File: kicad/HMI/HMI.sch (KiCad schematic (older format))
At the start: 38 parts

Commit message: Add files via upload
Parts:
- added R? (x6): 47k, symbol Device:R
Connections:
- net +3V3: now also R?.1, R?.1, R?.1, R?.1, R?.1, R?.1
- net R1: now also R?.2
- net R2: now also R?.2
- net R3: now also R?.2
- net R4: now also R?.2
- net R5: now also R?.2
- net R6: now also R?.2
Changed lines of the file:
@@
 	1    0    0    -1
 $EndComp
+Text GLabel 5900 2050 3    50   BiDi ~ 10
+R6
+$Comp
+L Device:R R?
+U 1 1 5E2A8493
+P 5900 1800
+F 0 "R?" H 5970 1846 50  0000 L CNN
+F 1 "47k" H 5970 1755 50  0000 L CNN
+F 2 "" V 5830 1800 50  0001 C CNN
+F 3 "~" H 5900 1800 50  0001 C CNN
+	1    5900 1800
+	1    0    0    -1
+$EndComp
+$Comp
+L power:+3.3V #PWR?
+U 1 1 5E2A8834
+P 5900 1450
+F 0 "#PWR?" H 5900 1300 50  0001 C CNN
+F 1 "+3.3V" H 5915 1623 50  0000 C CNN
+F 2 "" H 5900 1450 50  0001 C CNN
+F 3 "" H 5900 1450 50  0001 C CNN
+	1    5900 1450
+	1    0    0    -1
+$EndComp
+Text GLabel 6050 2050 3    50   BiDi ~ 10
+R5
+Text GLabel 6200 2050 3    50   BiDi ~ 10
+R4
+Text GLabel 6350 2050 3    50   BiDi ~ 10
+R3
+Text GLabel 6500 2050 3    50   BiDi ~ 10
+R2
+Text GLabel 6650 2050 3    50   BiDi ~ 10
+R1
+$Comp
+L Device:R R?
+U 1 1 5E2C0402
+P 6050 1800
+F 0 "R?" H 6120 1846 50  0000 L CNN
+F 1 "47k" H 6120 1755 50  0000 L CNN
+F 2 "" V 5980 1800 50  0001 C CNN
+F 3 "~" H 6050 1800 50  0001 C CNN
+	1    6050 1800
+	1    0    0    -1
+$EndComp
+$Comp
+L Device:R R?
+U 1 1 5E2C057A
+P 6200 1800
+F 0 "R?" H 6270 1846 50  0000 L CNN
+F 1 "47k" H 6270 1755 50  0000 L CNN
+F 2 "" V 6130 1800 50  0001 C CNN
+F 3 "~" H 6200 1800 50  0001 C CNN
+	1    6200 1800
+	1    0    0    -1
+$EndComp
+$Comp
+L Device:R R?
+U 1 1 5E2C0631
+P 6350 1800
+F 0 "R?" H 6420 1846 50  0000 L CNN
+F 1 "47k" H 6420 1755 50  0000 L CNN
+F 2 "" V 6280 1800 50  0001 C CNN
+F 3 "~" H 6350 1800 50  0001 C CNN
+	1    6350 1800
+	1    0    0    -1
+$EndComp
+$Comp
+L Device:R R?
+U 1 1 5E2C075F
+P 6500 1800
+F 0 "R?" H 6570 1846 50  0000 L CNN
+F 1 "47k" H 6570 1755 50  0000 L CNN
+F 2 "" V 6430 1800 50  0001 C CNN
+F 3 "~" H 6500 1800 50  0001 C CNN
+	1    6500 1800
+	1    0    0    -1
+$EndComp
+$Comp
+L Device:R R?
+U 1 1 5E2C0888
+P 6650 1800
+F 0 "R?" H 6720 1846 50  0000 L CNN
+F 1 "47k" H 6720 1755 50  0000 L CNN
+F 2 "" V 6580 1800 50  0001 C CNN
+F 3 "~" H 6650 1800 50  0001 C CNN
+	1    6650 1800
+	1    0    0    -1
+$EndComp
+Wire Wire Line
+	5900 2050 5900 1950
+Wire Wire Line
+	6050 1950 6050 2050
+Wire Wire Line
+	6200 2050 6200 1950
+Wire Wire Line
+	6350 1950 6350 2050
+Wire Wire Line
+	6500 2050 6500 1950
+Wire Wire Line
+	6650 1950 6650 2050
+Wire Wire Line
+	6650 1650 6650 1550
+Wire Wire Line
+	6650 1550 6500 1550
+Wire Wire Line
+	5900 1550 5900 1450
+Wire Wire Line
+	5900 1650 5900 1550
+Connection ~ 5900 1550
+Wire Wire Line
+	6050 1550 6050 1650
+Connection ~ 6050 1550
+Wire Wire Line
+	6050 1550 5900 1550
+Wire Wire Line
+	6200 1550 6200 1650
+Connection ~ 6200 1550
+Wire Wire Line
+	6200 1550 6050 1550
+Wire Wire Line
+	6350 1550 6350 1650
+Connection ~ 6350 1550
+Wire Wire Line
+	6350 1550 6200 1550
+Wire Wire Line
+	6500 1550 6500 1650
+Connection ~ 6500 1550
+Wire Wire Line
+	6500 1550 6350 1550
 $EndSCHEMATC

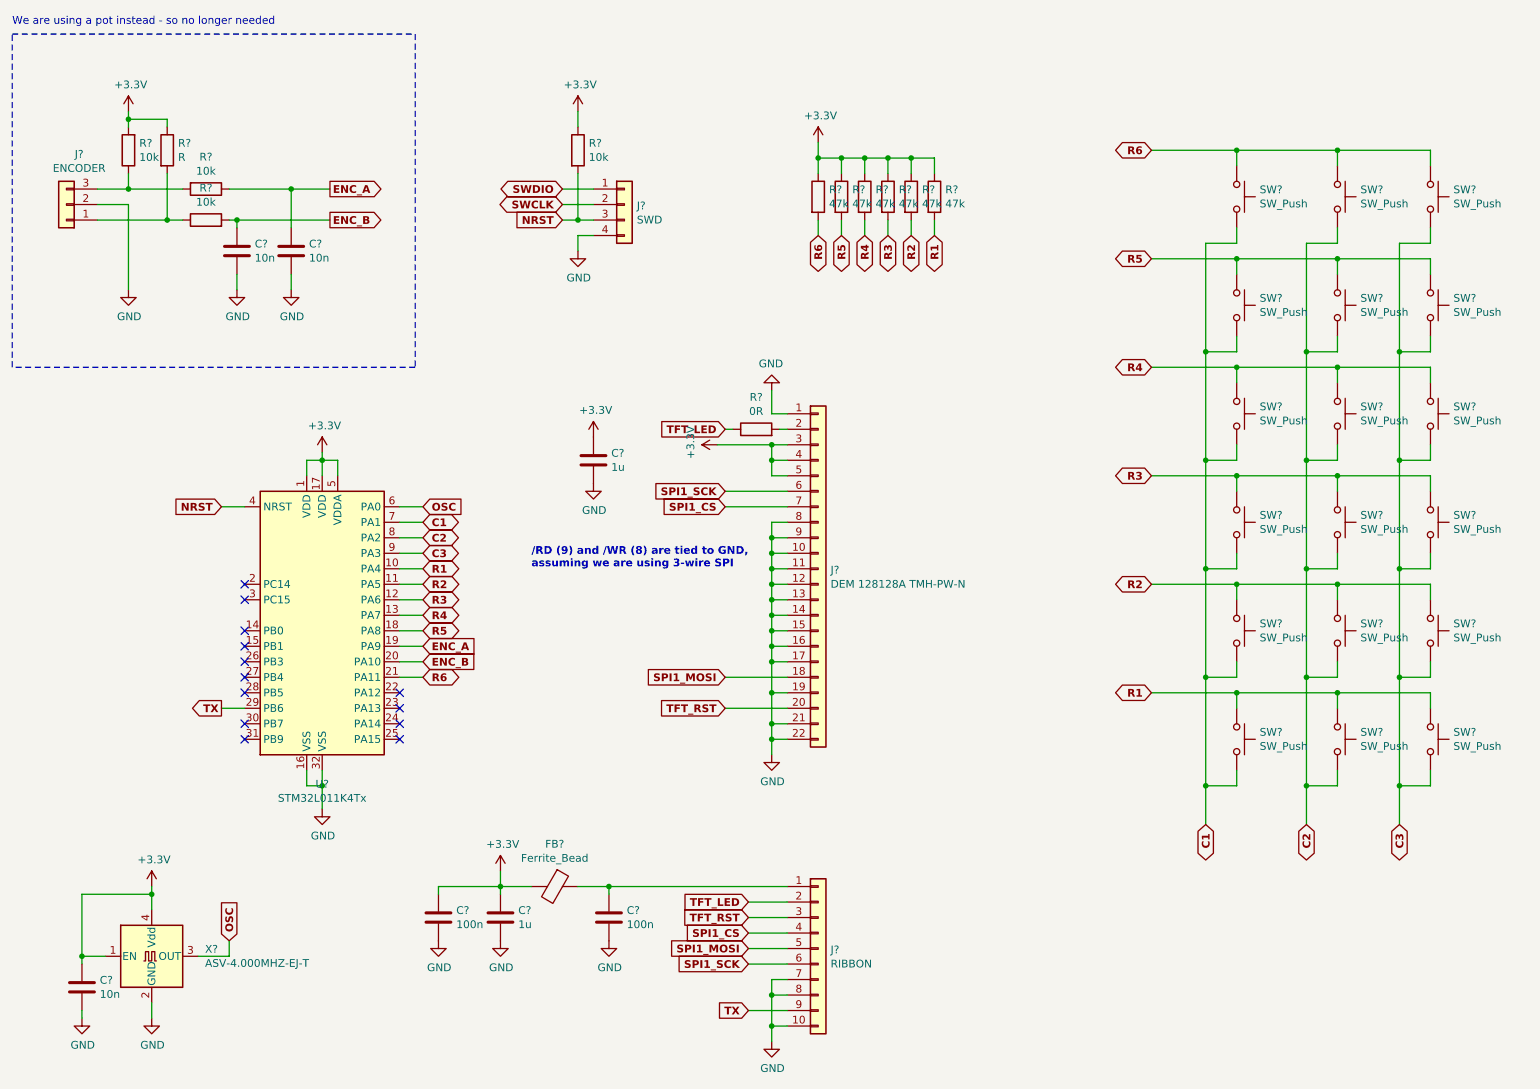
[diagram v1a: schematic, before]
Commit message: Add files via upload
added 2 buttons: F1 and F2
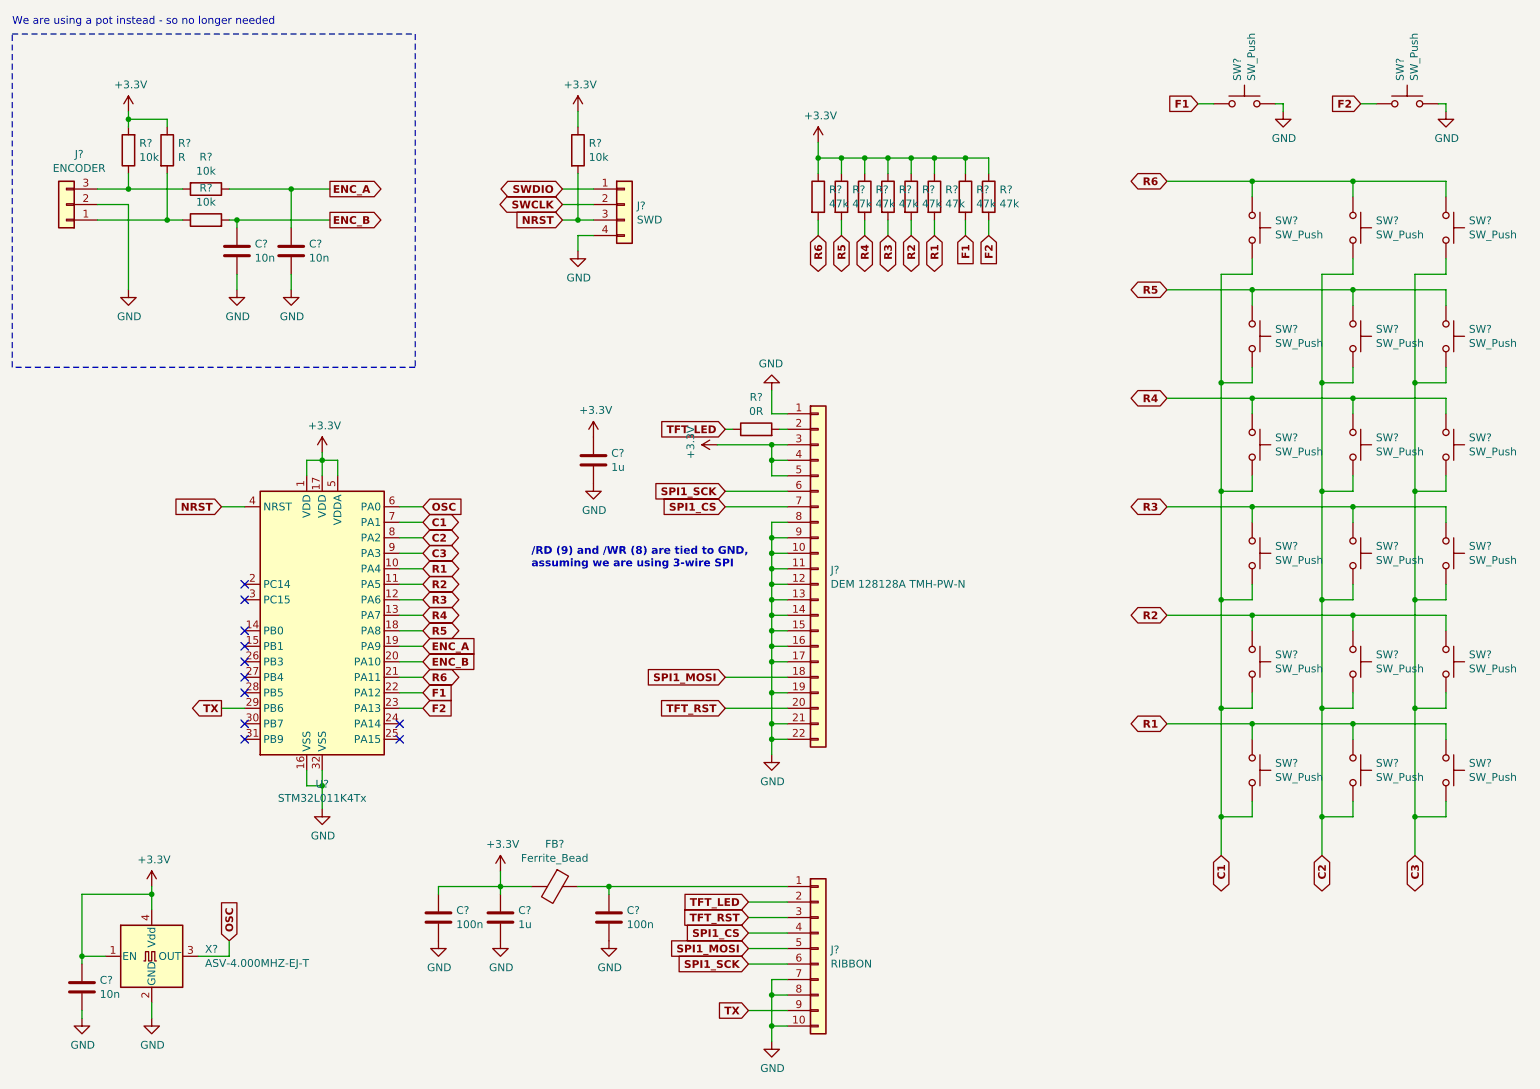
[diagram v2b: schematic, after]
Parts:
- added R? (x2): 47k, symbol Device:R
- added SW? (x2): SW_Push, symbol Switch:SW_Push
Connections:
- net +3V3: now also R?.1, R?.1
- net GND: now also SW?.2, SW?.2
- net F1: now reaches U?.22 (PA12)
- net F1: now also R?.2, SW?.1
- net F2: now reaches U?.23 (PA13)
- net F2: now also R?.2, SW?.1
- no-connect marks 13 -> 11
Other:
- moved on the sheet: SW?

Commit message: Add files via upload
i've set some footprints and changed that 10-pin connector pin order
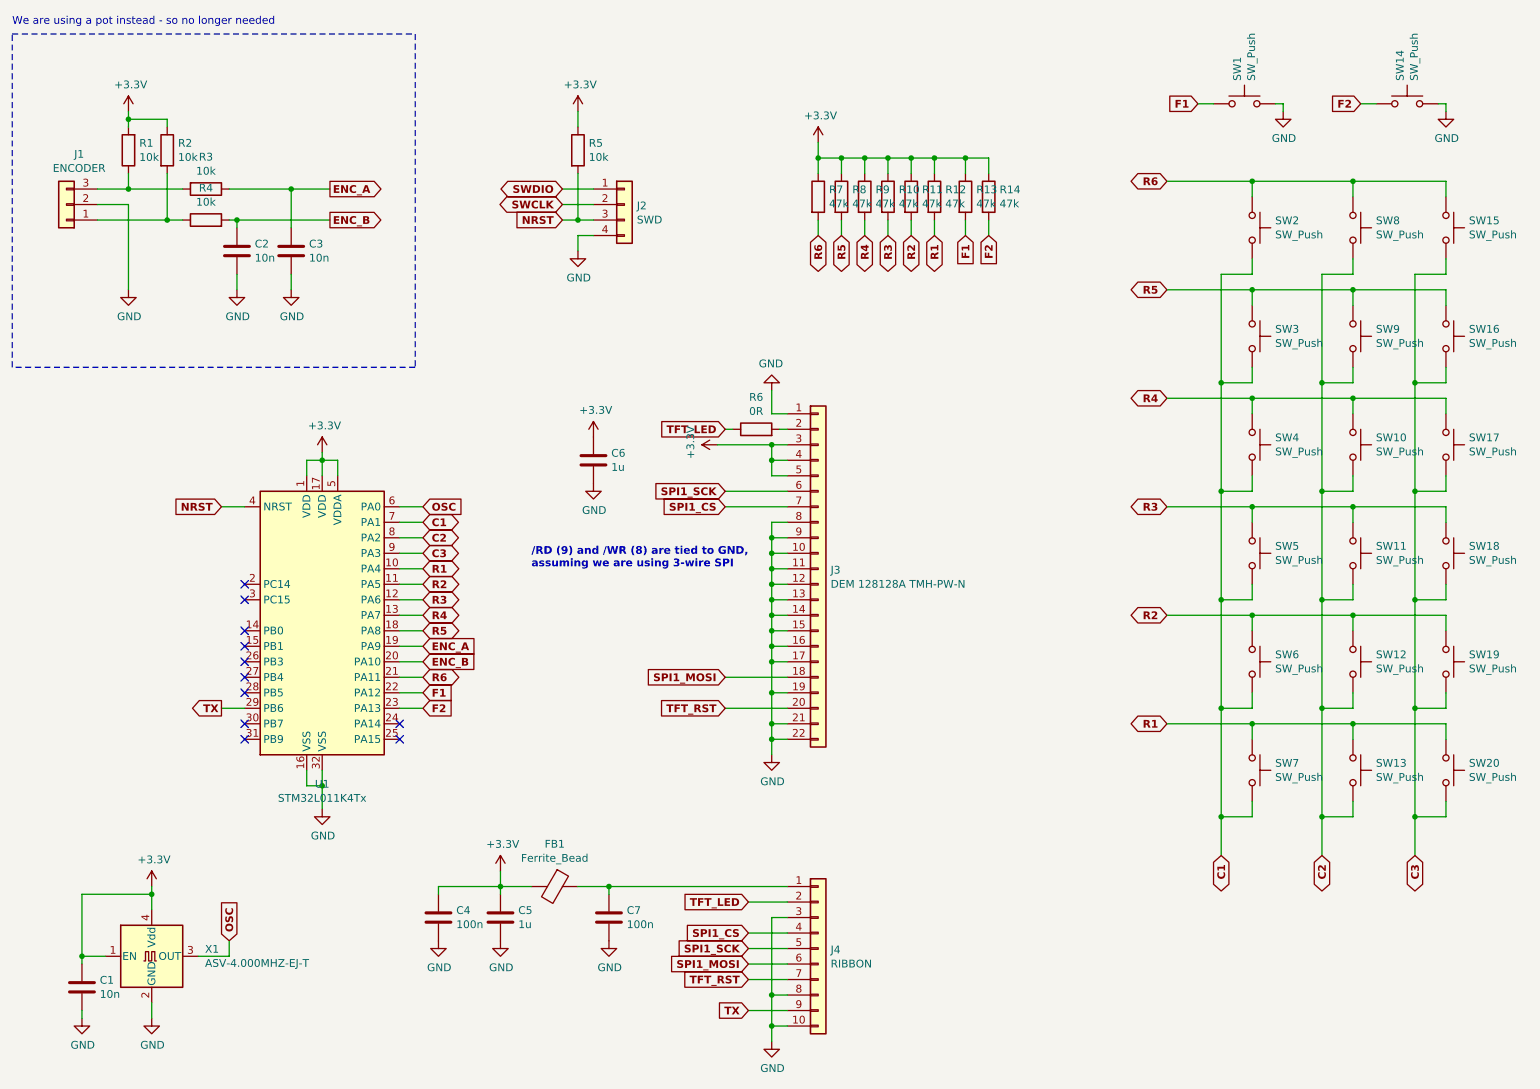
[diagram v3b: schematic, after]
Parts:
- C1, C2, C3, C4, C5, C6, C7: renamed from C?; footprint (none) -> Capacitor_SMD:C_0603_1608Metric
- FB1: renamed from FB?; footprint (none) -> Inductor_SMD:L_0603_1608Metric
- J1: renamed from J?; footprint (none) -> Connector_PinSocket_2.54mm:PinSocket_1x03_P2.54mm_Vertical
- J2: renamed from J?; footprint (none) -> Connector_PinSocket_2.54mm:PinSocket_1x04_P2.54mm_Vertical
- R1, R10, R11, R12, R13, R14, R3, R4, R5, R6, R7, R8, R9: renamed from R?; footprint (none) -> Resistor_SMD:R_0603_1608Metric
- R2: renamed from R?; value R -> 10k; footprint (none) -> Resistor_SMD:R_0603_1608Metric
- gave numbers to parts that had none: 24
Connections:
- net GND: now also J4.3 (Pin_3); no longer J4.7 (Pin_7)
- net SPI1_MOSI: now also J4.6 (Pin_6); no longer J4.5 (Pin_5)
- net SPI1_SCK: now also J4.5 (Pin_5); no longer J4.6 (Pin_6)
- net TFT_RST: now also J4.7 (Pin_7); no longer J4.3 (Pin_3)
